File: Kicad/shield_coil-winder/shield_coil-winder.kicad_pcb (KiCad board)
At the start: 2 copper layers, 68.6 x 89.4 mm, 32 parts, among them K1 SOCKET_DRIVER_B, K2 SOCKET_DRIVER_A, P1 Power, P10 MicroSteps, P11 MOTOR-B, P12 MOTOR-A, P13 ALIM_EXT, P2 Analog, P3 Digital, P4 Digital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

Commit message: V1.1 pcb
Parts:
- added D4: LED, LEDs:LED-3MM, F.Cu at (123.2, 110.1)
- added R6: 10K, Resistors_ThroughHole:Resistor_Horizontal_RM10mm, F.Cu at (136.3, 110.1)
- F1: value 3A -> MF-R050
- K1: value SOCKET_DRIVER_B -> SOCKET_DRIVER_A
- K2: value SOCKET_DRIVER_A -> SOCKET_DRIVER_B
- P11: value MOTOR-B -> MOTOR-A
- P12: value MOTOR-A -> MOTOR-B
- moved SW2 6.18 mm to (129.1, 119.6), turned to 0 degrees
- moved R5 0.25 mm to (169.9, 92.1)
- moved K1 0.13 mm to (130.8, 93.5)
- moved K2 0.13 mm to (154.9, 93.5)
- moved SW1 0.07 mm to (167.1, 114.3)
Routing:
- net GND: track 295.5 -> 396.8 mm
- net Net-(D4-Pad1): track 0.00 -> 2.92 mm
- net VCC: track 92.5 -> 94.2 mm
- net /SW-ENC_4: track 56.0 -> 55.1 mm
- net RESET: track 18.5 -> 17.7 mm
- net /IT_3: track 38.8 -> 38.2 mm
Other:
- board text added: "+"
- board text added: "321"
- board text added: "Dir"
- board text added: "EN"
- board text added: "M-A"
- board text added: "M-B"
- board text added: "Micro"
- board text added: "Shield : Coil Winder v1.1"
- board text added: "Vcc"
- board text added: "gnd"
- board text added: "|||"
- board text removed: "Shield : Coil Winder v1.0"

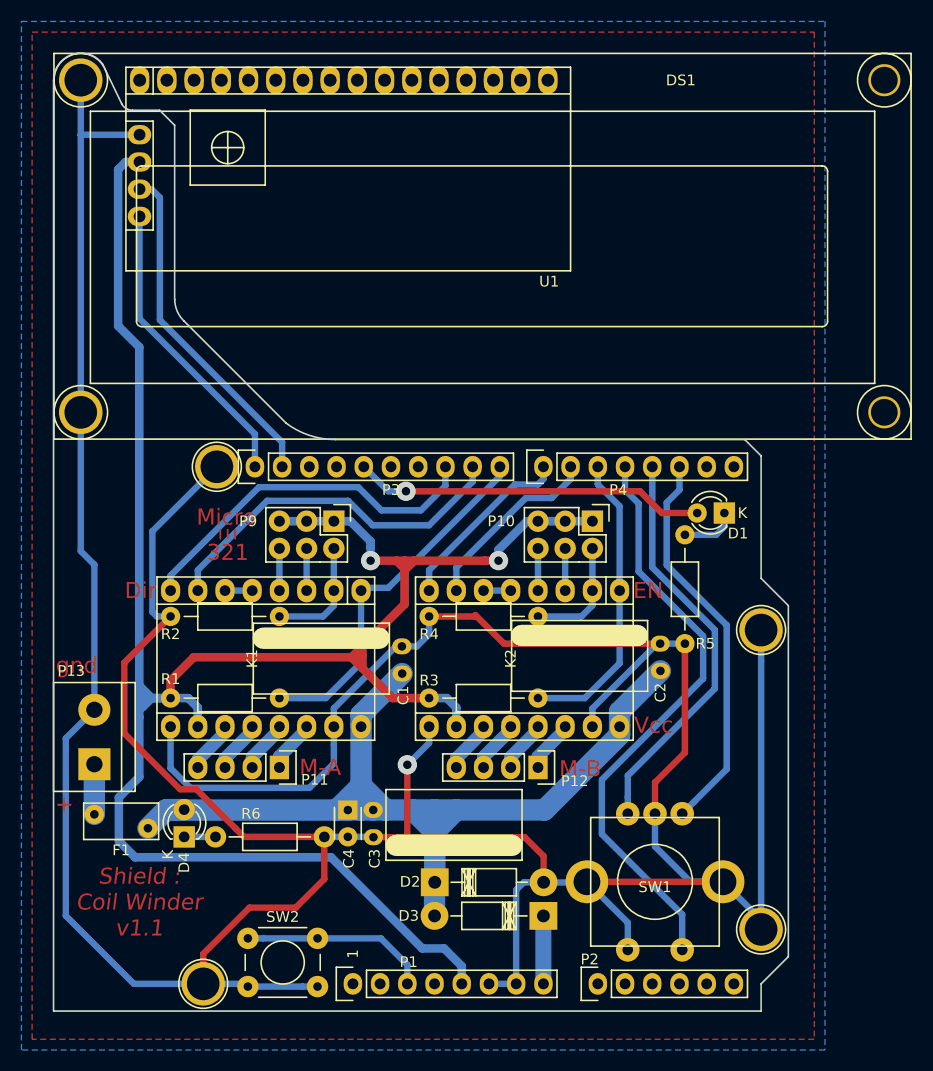
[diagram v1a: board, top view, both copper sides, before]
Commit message: Correction label pin on sockets
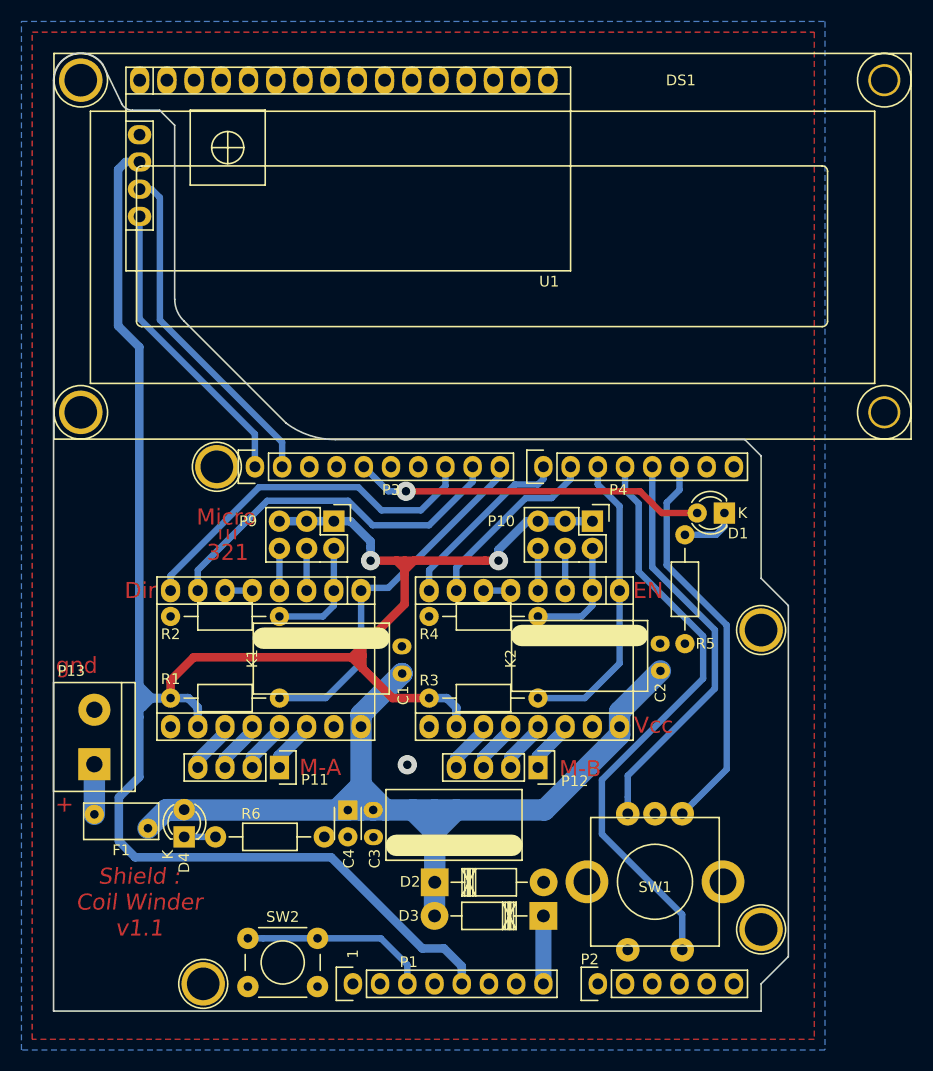
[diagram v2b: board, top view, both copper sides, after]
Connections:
- net /DIR-A_7 renamed /DIR-B_7
- net /DIR-B_10 renamed /DIR-A_10
- net /EN-A_5 renamed /EN-B_5
- net /EN-B_8 renamed /EN-A_8
- net /STEP-A_6 renamed /STEP-B_6
- net /STEP-B_9 renamed /STEP-A_9
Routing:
- net GND: track 396.8 -> 3.20 mm, vias 1 -> 0
- net (no net): vias 0 -> 1
